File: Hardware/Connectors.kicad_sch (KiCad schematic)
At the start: 21 parts, among them IC5 USBLC6-2SC6, J1 SWD header, J2 216990-0003, J3 MEM2061-01-188-00-A, Q1 BSS316NH6327XTSA1

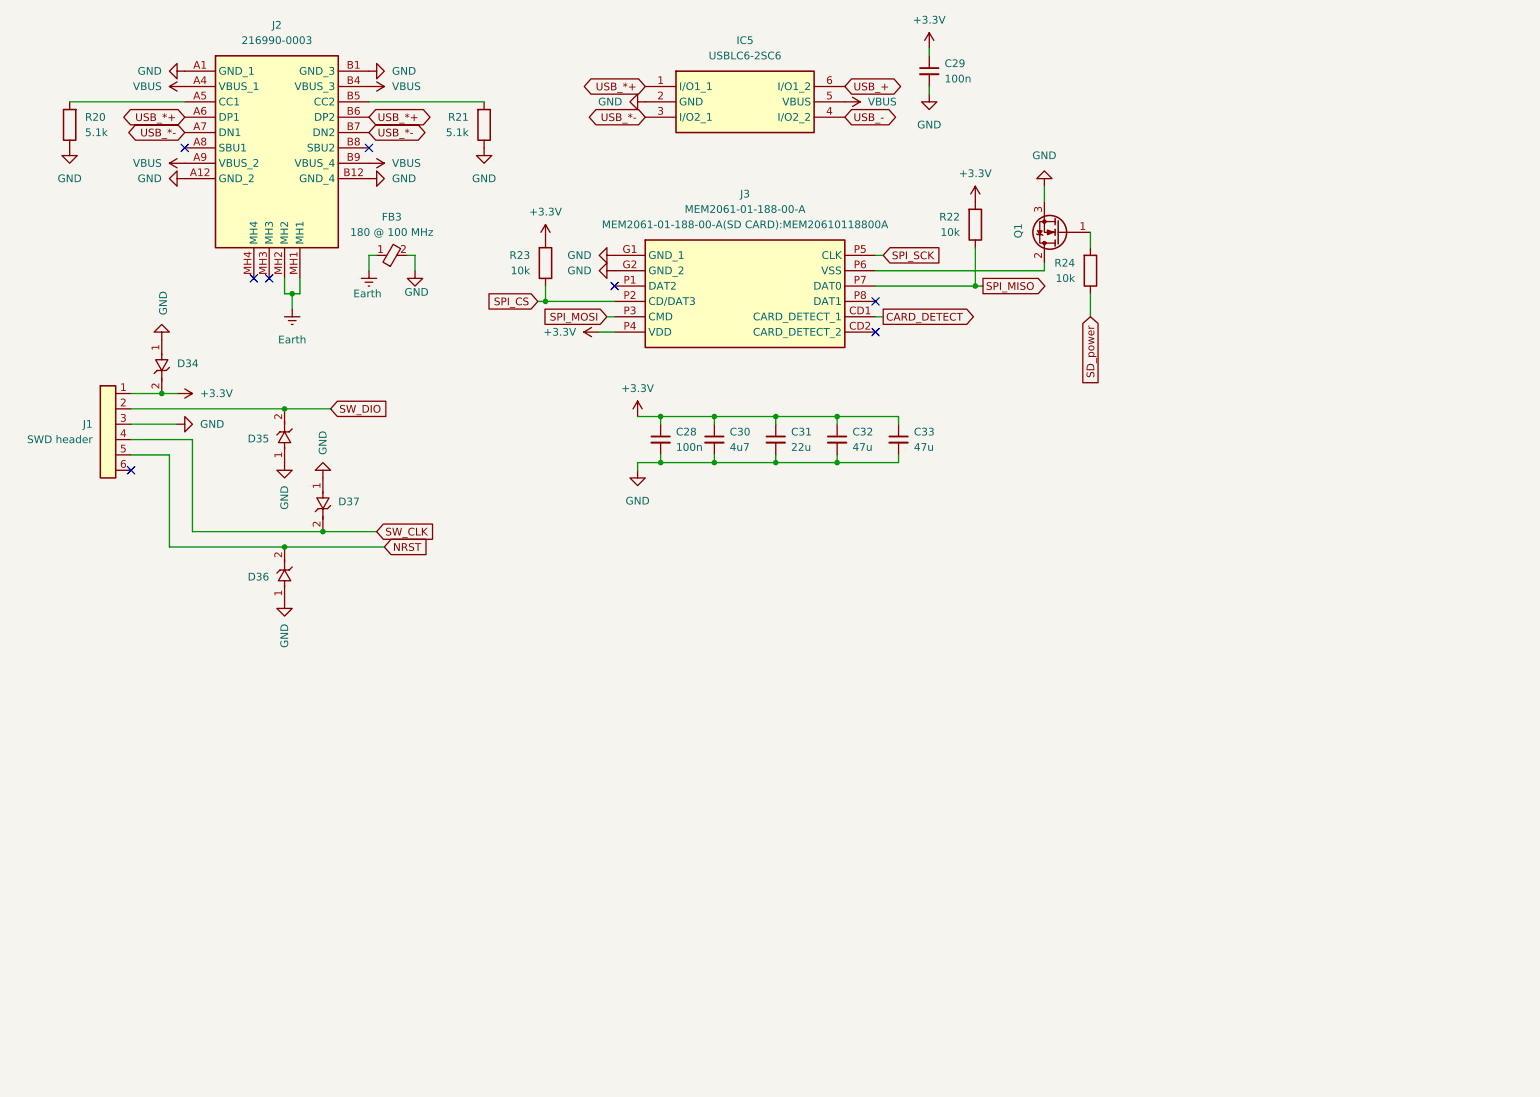
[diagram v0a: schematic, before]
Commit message: updated files, added PDF versions on schematic and PCB
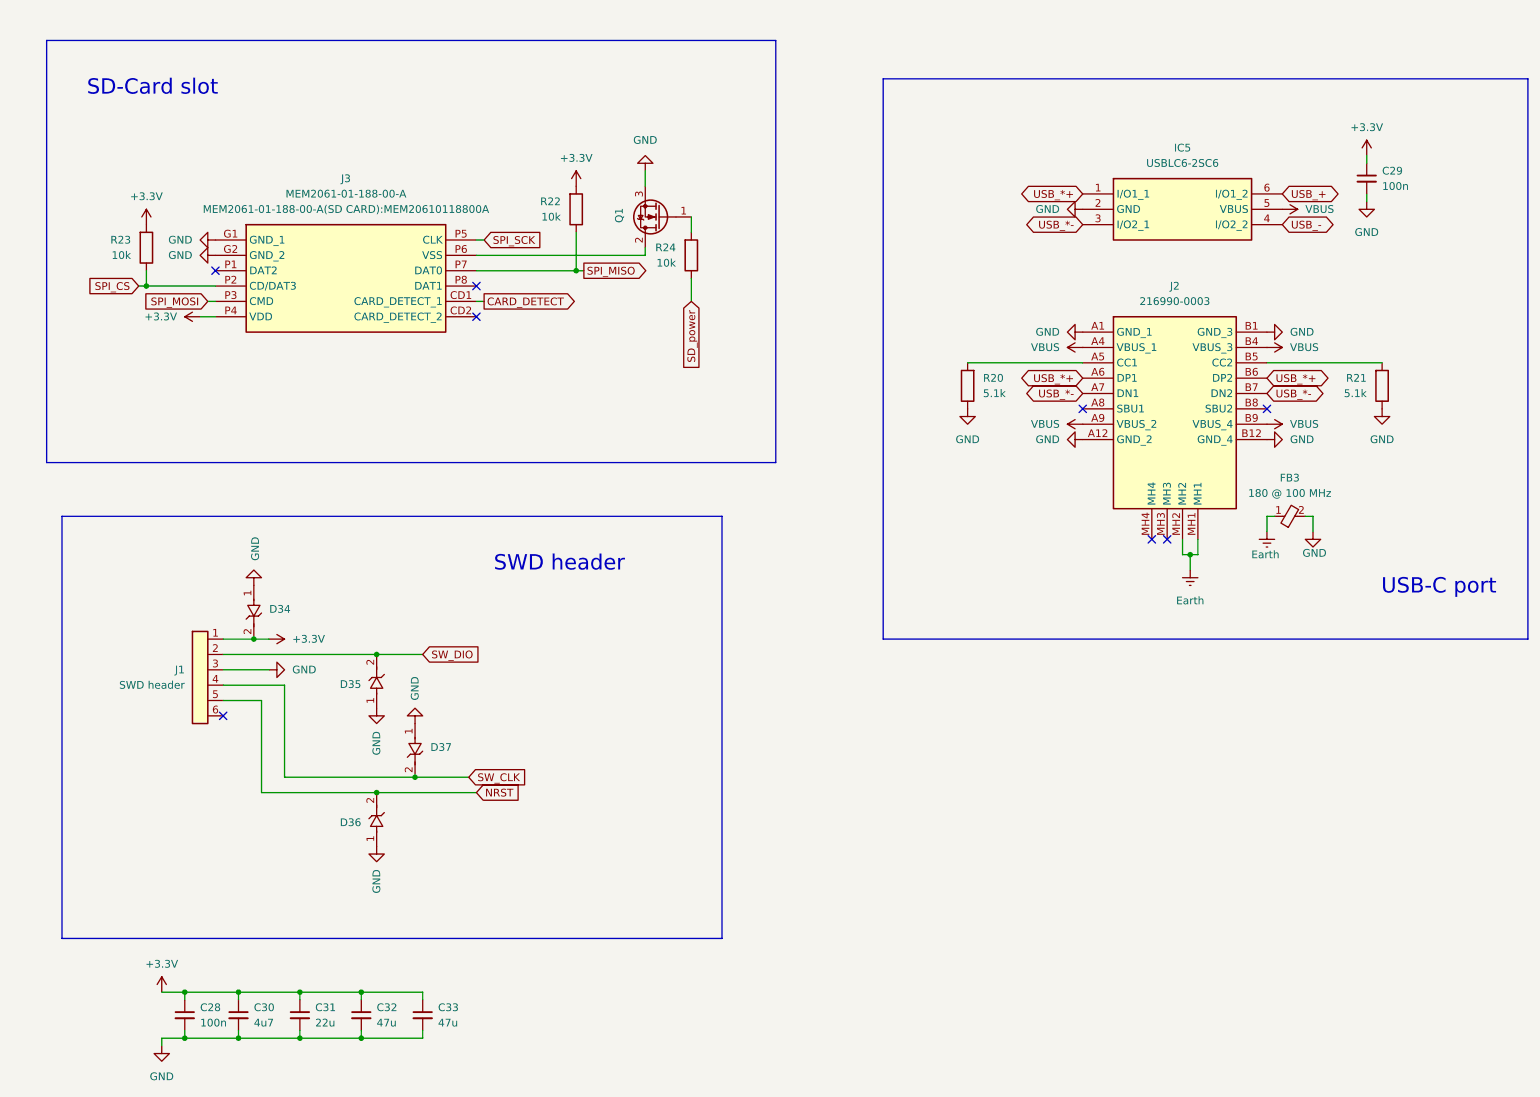
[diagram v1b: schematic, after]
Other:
- note added: "SD-Card slot"
- note added: "SWD header"
- note added: "USB-C port"
- moved on the sheet: C28, C29, C30, C31, C32, C33, D34, D35, D36, D37, FB3, IC5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
